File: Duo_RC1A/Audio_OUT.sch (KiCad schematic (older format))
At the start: 41 parts, among them J3 JACK_P10_TRS_6P, J4 JACK_P10_TRS_6P, J5 JACK_P10_TRS_6P, K1 IMC03TS, K2 IMC03TS, Q1 BS870, Q2 BS870, Q3 BS870

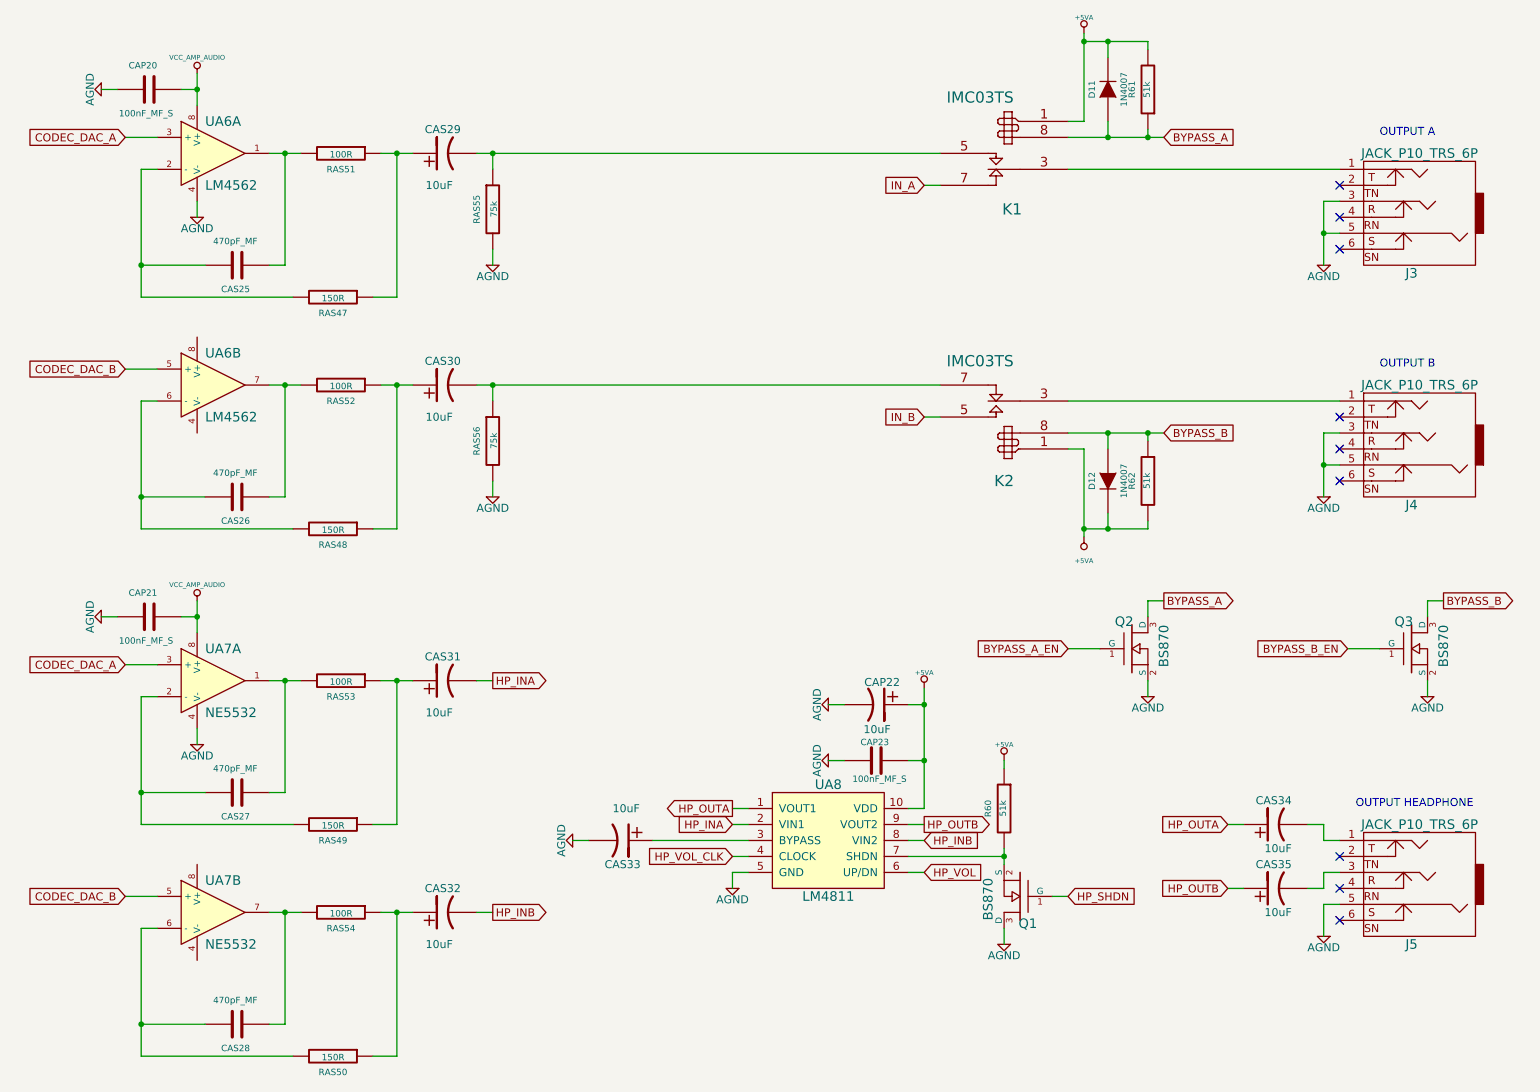
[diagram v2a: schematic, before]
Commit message: Rear pannel layout finished. First layout of sound modules.
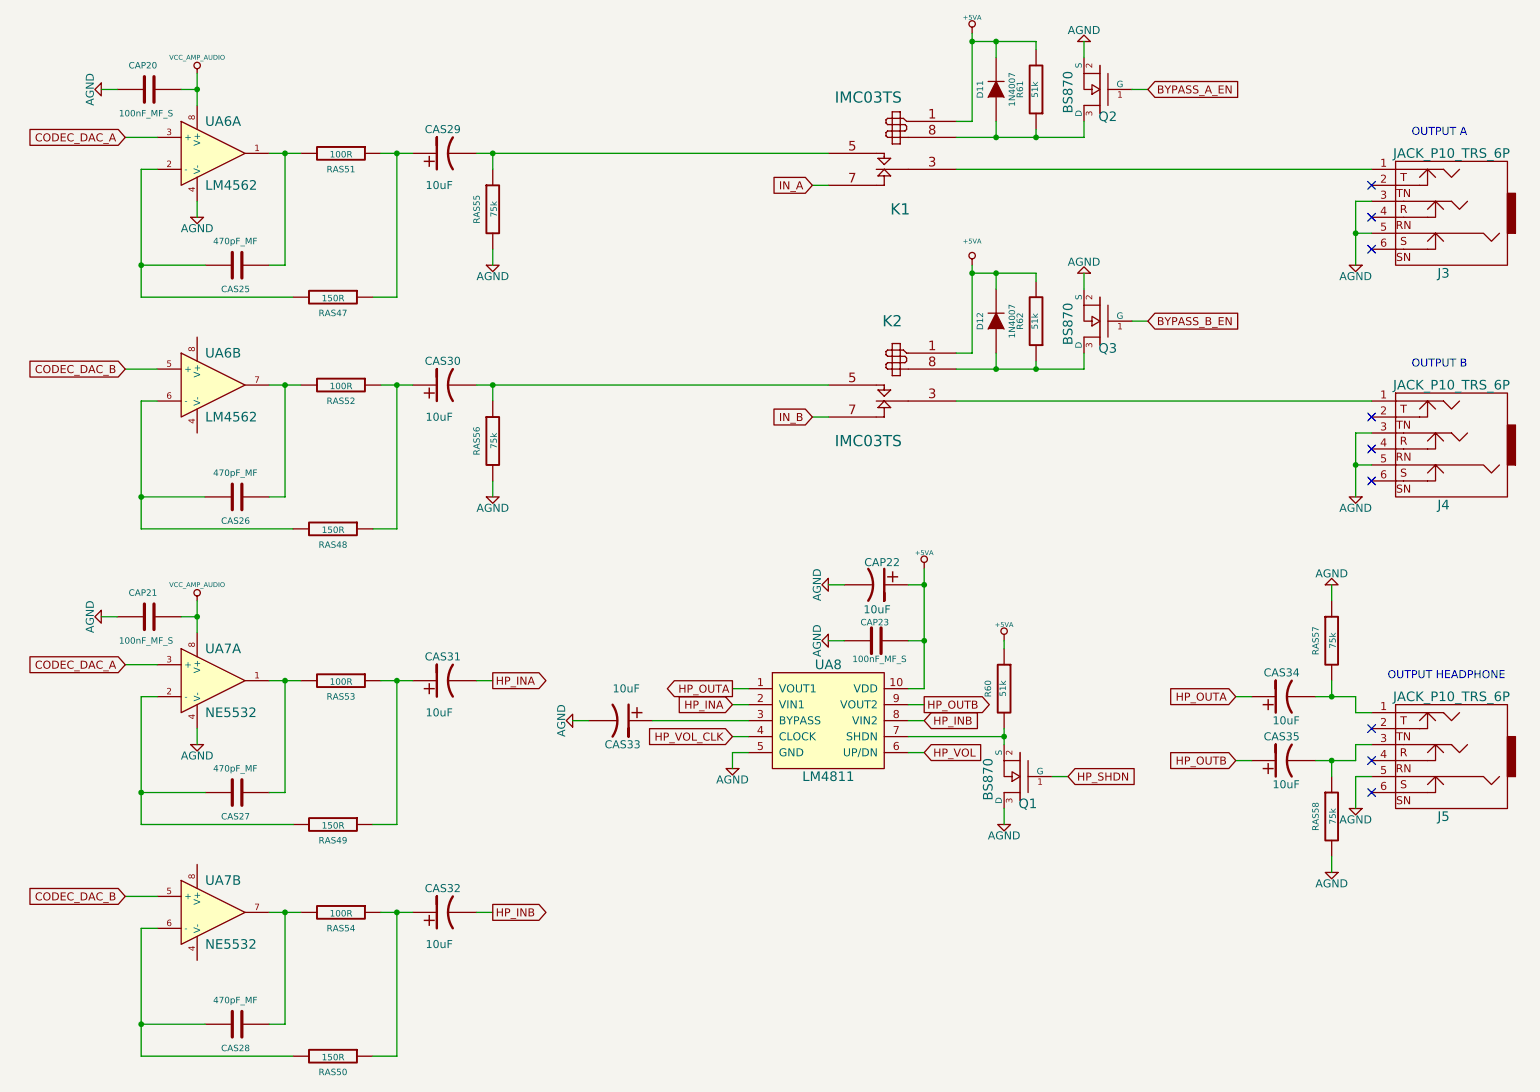
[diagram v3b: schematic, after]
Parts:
- added RAS57, RAS58: 75k, Duo_Audio_HMI_RC1A:Resistor_PTH_6.35x2.35mm, symbol R
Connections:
- net AGND: now also RAS57.1, RAS58.2
- net IN_B: now also K2.7 (R); no longer K2.5 (T)
- net at CAS30.2, RAS56.1: now also K2.5 (T); no longer K2.7 (R)
- net at CAS34.2, J5.1: now also RAS57.2
- net at CAS35.2, J5.3: now also RAS58.1
- net BYPASS_A: no longer names the net of D11.1 (A), K1.8, Q2.3 (D), R61.1
- net BYPASS_B: no longer names the net of D12.1 (A), K2.8, Q3.3 (D), R62.1
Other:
- moved on the sheet: CAP22, CAP23, CAS33, CAS34, CAS35, D11, D12, J3, J4, J5, K1, K2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

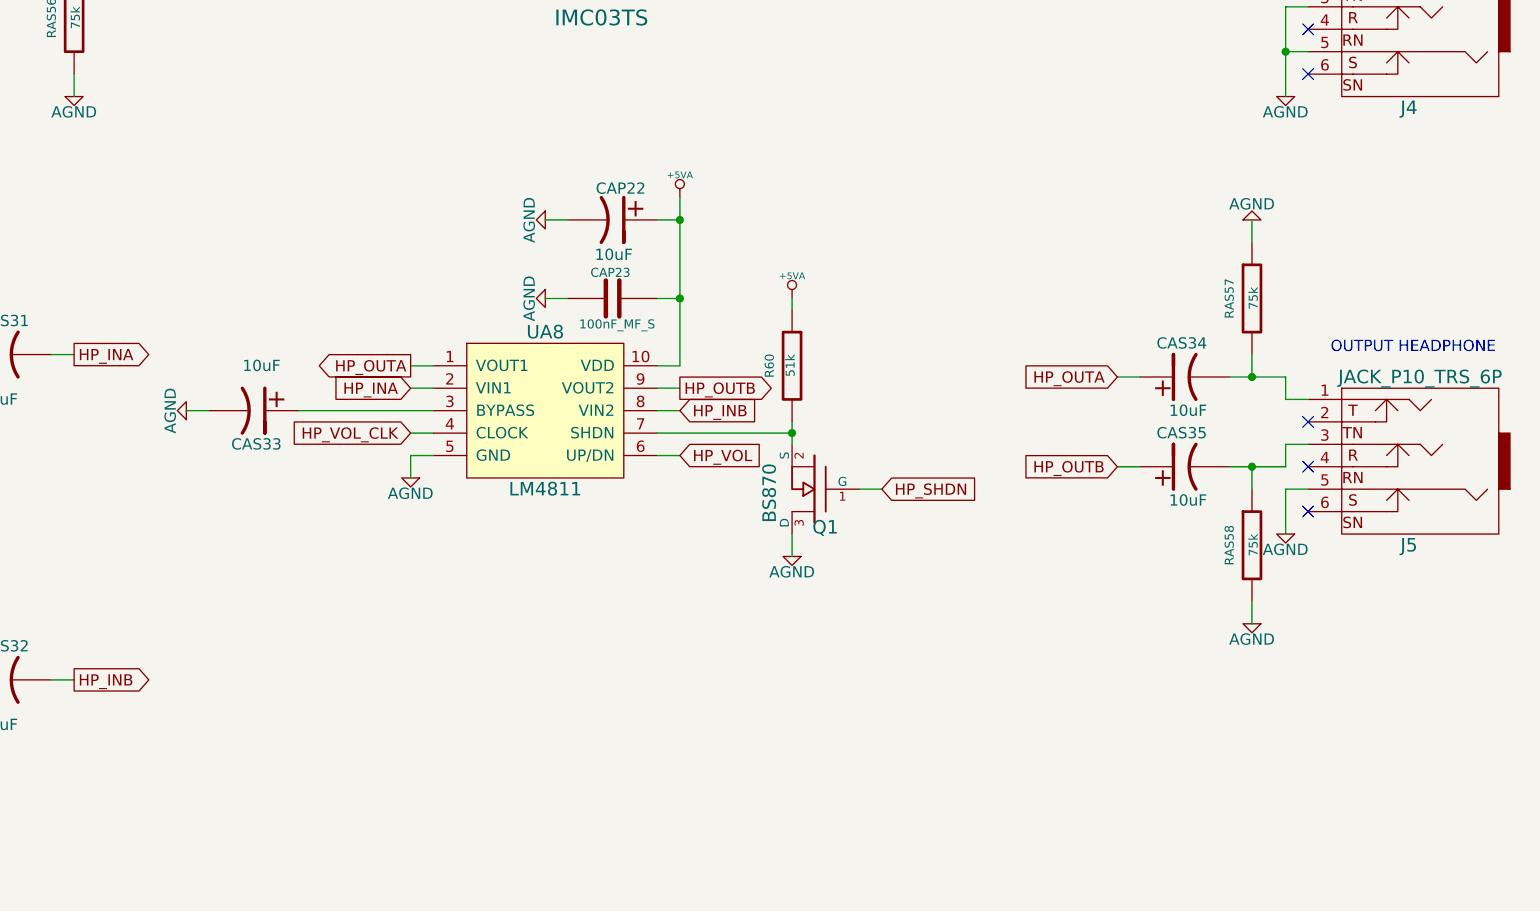
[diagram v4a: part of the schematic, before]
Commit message: Removed CODEC_MITEC signal. Defined the connector between the TopBoard and the BottomBoard. Saved layouts in *.brd old format.
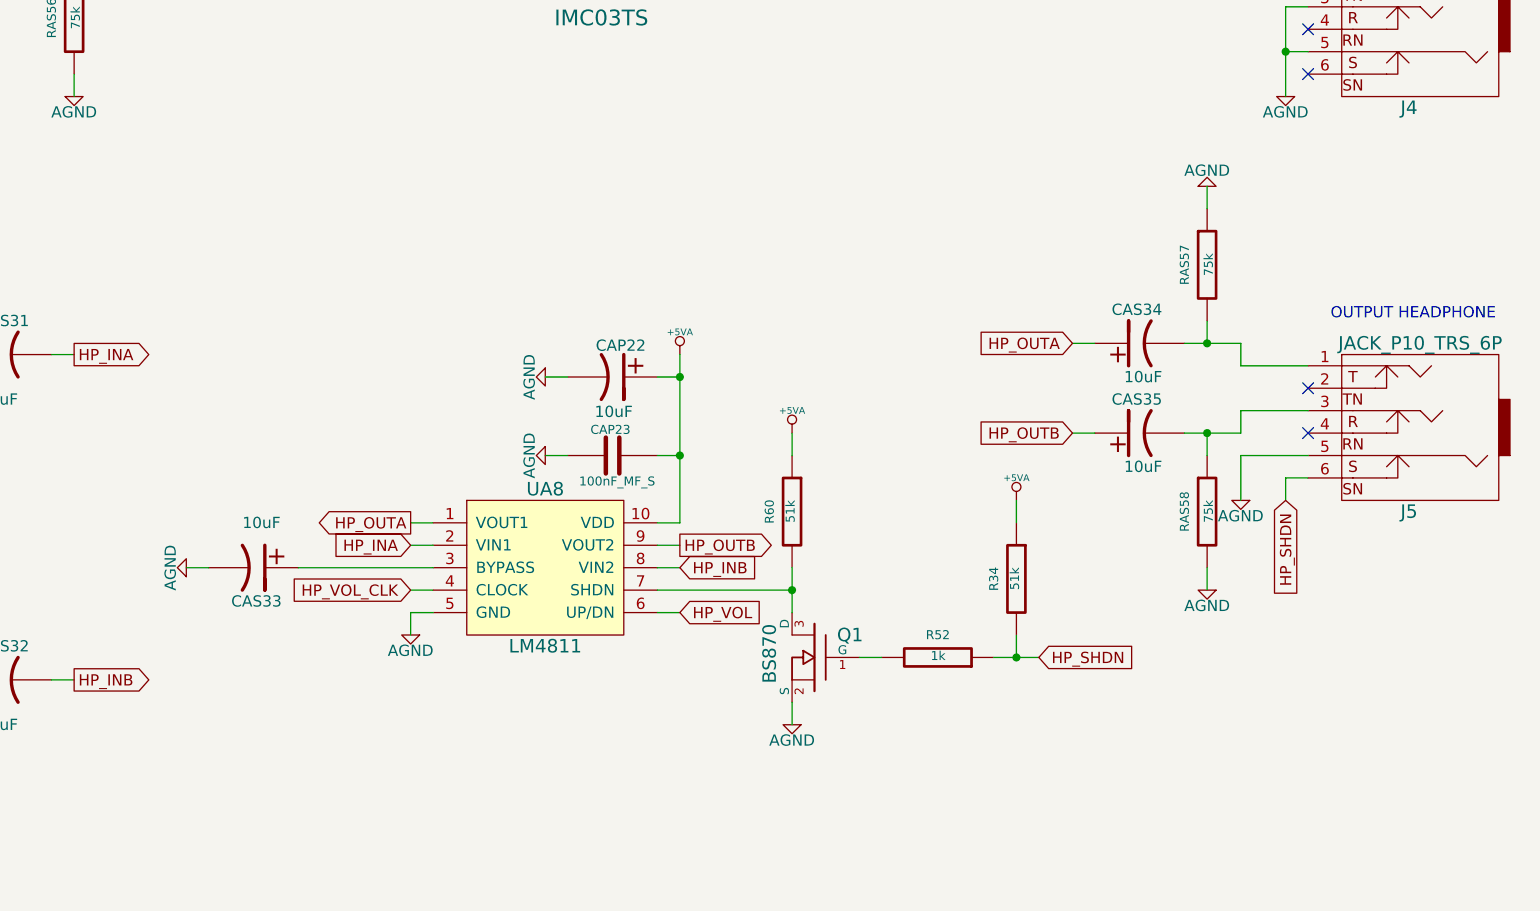
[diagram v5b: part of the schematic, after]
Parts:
- added R34: 51k, Duo_Audio_HMI_RC1A:SM0603, symbol R
- added R52: 1k, Duo_Audio_HMI_RC1A:SM0603, symbol R
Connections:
- net +5VA: now also R34.1
- net AGND: now also Q1.2 (S); no longer Q1.3 (D)
- net HP_SHDN: now also J5.6, R34.2, R52.1; no longer Q1.1 (G)
- net at R60.2, UA8.7 (SHDN): now also Q1.3 (D); no longer Q1.2 (S)
- new net: Q1.1 (G), R52.2
- no-connect marks 9 -> 8
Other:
- moved on the sheet: CAP22, CAP23, CAS33, CAS34, CAS35, J5, R60, RAS57, RAS58, UA8
